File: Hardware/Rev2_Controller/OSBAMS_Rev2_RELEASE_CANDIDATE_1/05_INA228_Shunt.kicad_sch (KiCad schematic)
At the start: 14 parts, among them J5 SHUNT_KELVIN, U2 INA228

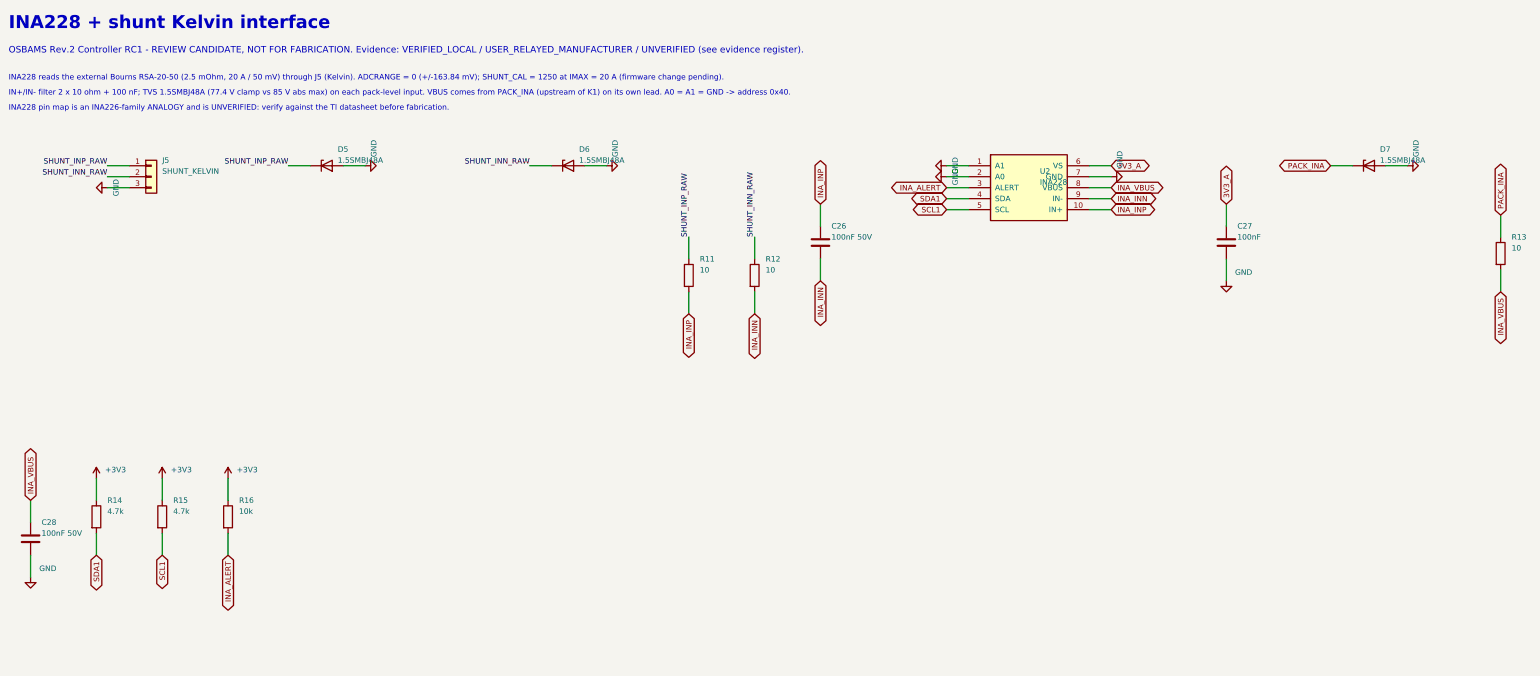
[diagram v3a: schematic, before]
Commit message: RC1.2: pack-sense surge resistors, isolation/clearance rules, buck envelope, evidence classification, no shipped Gerbers
- R41 47R (PACK_INA) and R42/R43 10R (Kelvin lines) upstream of the 1.5SMBJ48A diodes; credible-transient analysis with simulation (PASS)
- custom DRC rules: host-to-controller >= 1.0 mm on every layer, INA228 fine-pitch exemption; pack-level class 0.2 mm (IPC-2221B B4 basis)
- isolation audit per layer with coordinates; XDR 12.0 V / max continuous input 14.4 V; IRLML0060 margin estimate + mandatory first-article checks
- board re-routed: ERC 0, DRC 0, unconnected 0, netlist 0 mismatches (403 pads); silkscreen warnings fixed
- script-generated Gerbers/drills removed from the package; BOM adds qty for 5 boards and MPN suffix status; new evidence-risk, connector-check and pre-PCBWay checklist documents

Co-Authored-By: Claude Sonnet 5.5 <noreply@anthropic.com>
Claude-Session: https://claude.ai/code/session_01HV1TCrYnLTcNjmYdFqCPLo
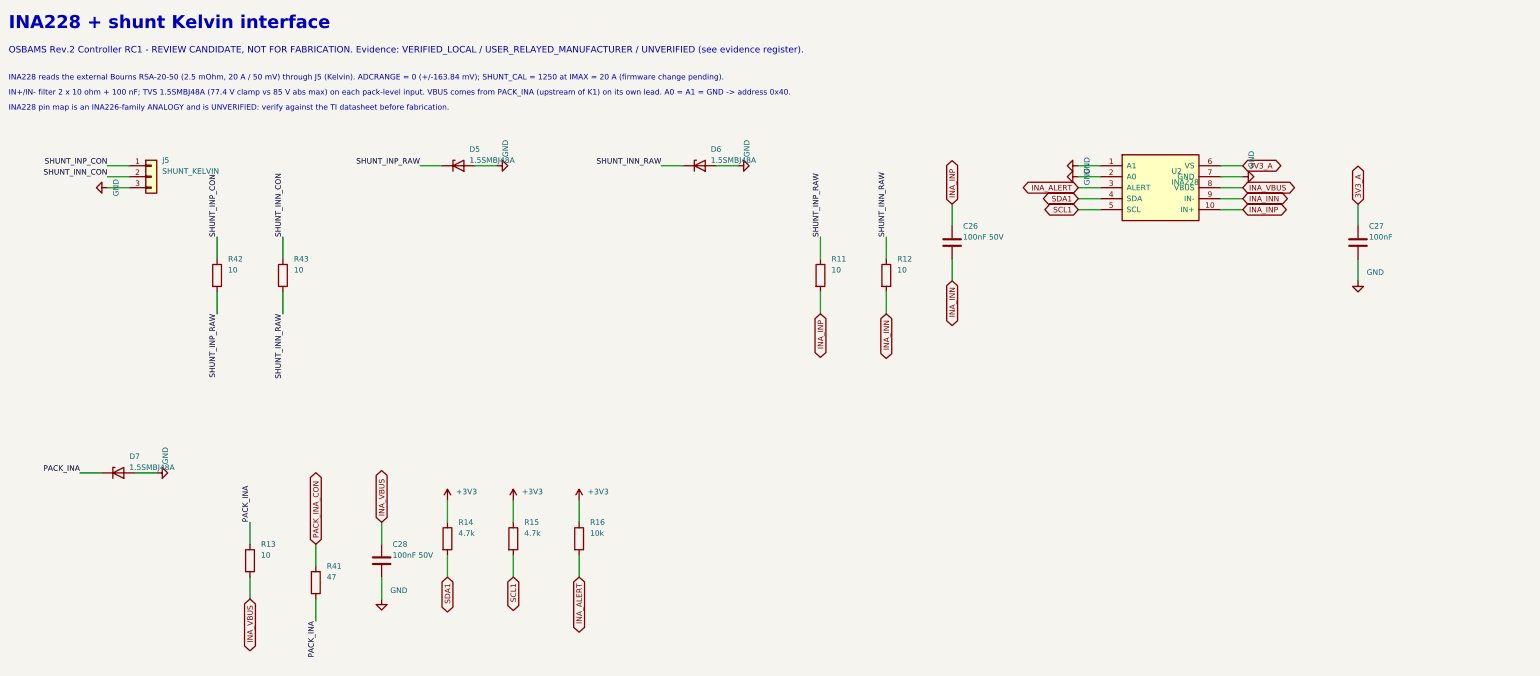
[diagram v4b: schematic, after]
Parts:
- added R41: 47, Resistor_SMD:R_1206_3216Metric, symbol Device:R
- added R42, R43: 10, Resistor_SMD:R_1206_3216Metric, symbol Device:R
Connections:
- net PACK_INA: now also R41.2
- net SHUNT_INN_RAW: now also R43.2; no longer J5.2 (Pin_2)
- net SHUNT_INP_RAW: now also R42.2; no longer J5.1 (Pin_1)
- new net PACK_INA_CON: R41.1
- new net SHUNT_INN_CON: J5.2 (Pin_2), R43.1
- new net SHUNT_INP_CON: J5.1 (Pin_1), R42.1

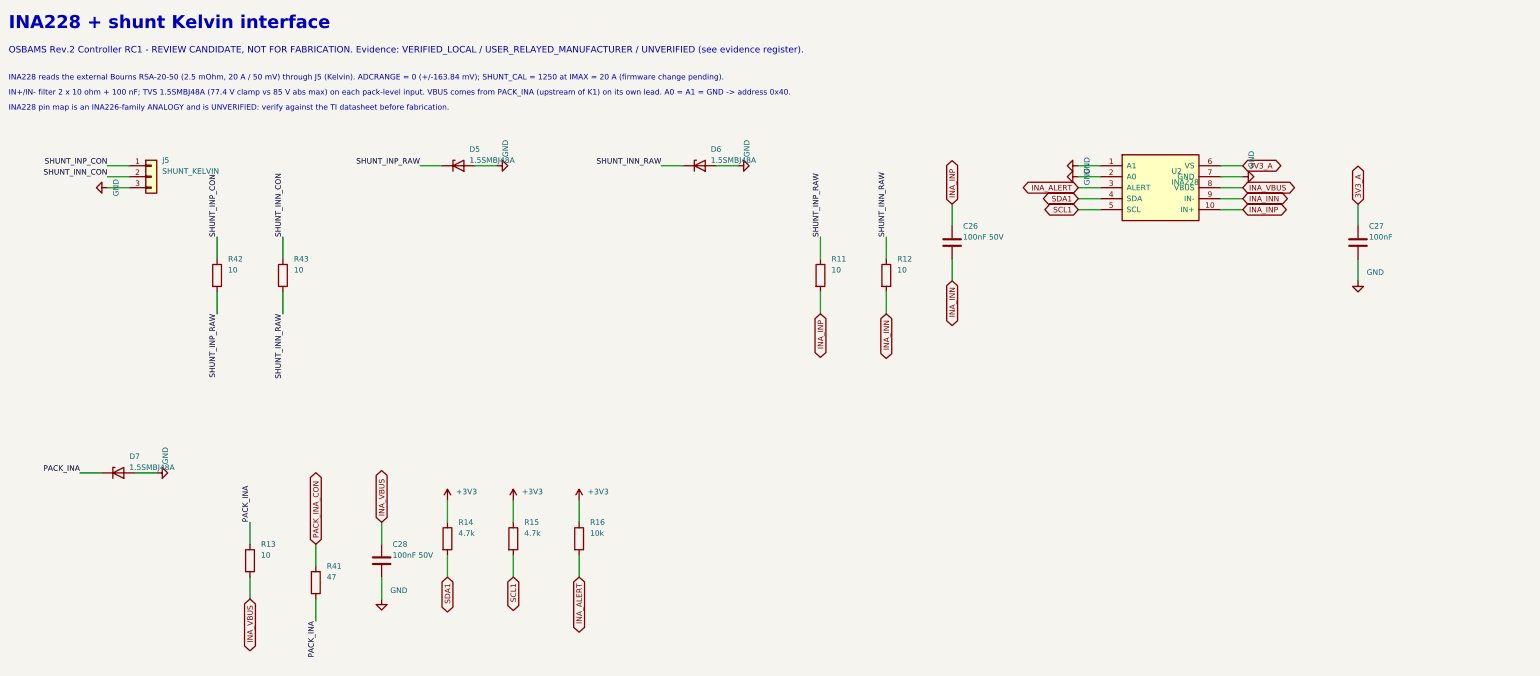
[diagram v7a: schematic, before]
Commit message: RC1.2e: Samtec J9 land pattern (0.74x2.79, rev H), D15 differential clamp across INA228 IN+/IN-, protection and connector audit; ERJ-P08 pulse capability re-opened
- J9 generic footprint replaced by OSBAMS_Rev2:FTSH-105-01-L-DV-K from the Samtec recommended layout rev H; breakout re-routed
- D15 SMF12CA bidirectional TVS across INA_INP/INA_INN (INA228 differential limit +/-40 V; one Kelvin lead open)
- CONTROLLER_PROTECTION_AND_CONNECTOR_AUDIT.md (PASS / CHANGE REQUIRED / FIRST-ARTICLE VALIDATION / REMAINING FABRICATION BLOCKERS)
- rs_pulse_rating back to UNVERIFIED/critical; Molex J5/J6 stay open (3D drawing without dimensions); evidence PDFs committed
- ERC 0, DRC 0, unconnected 0, netlist 0 mismatches (405 pads), polarity OK, isolation >= 1.0 mm; 181 tests pass

Co-Authored-By: Claude Sonnet 5.5 <noreply@anthropic.com>
Claude-Session: https://claude.ai/code/session_01HV1TCrYnLTcNjmYdFqCPLo
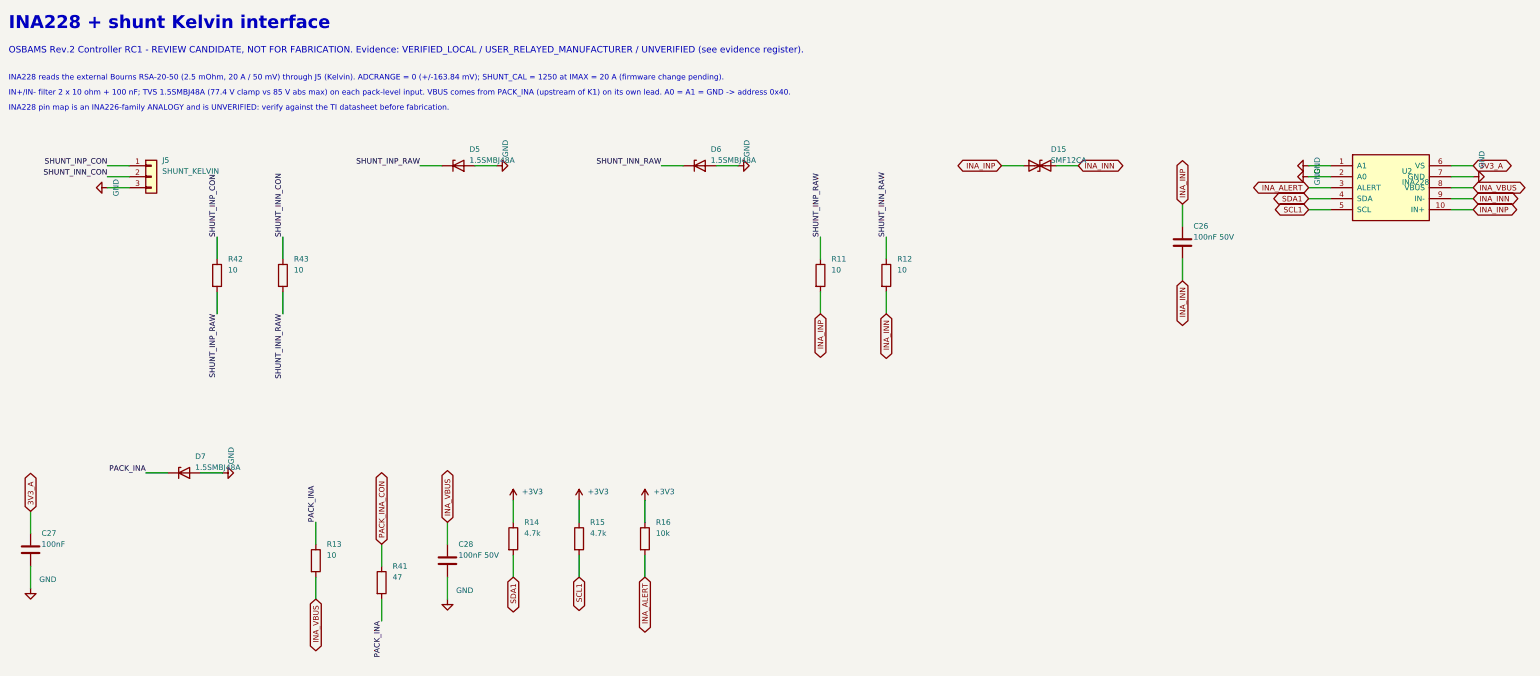
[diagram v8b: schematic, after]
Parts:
- added D15: SMF12CA, Diode_SMD:D_SMF, symbol Device:D_TVS
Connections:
- net INA_INN: now also D15.2 (A2)
- net INA_INP: now also D15.1 (A1)
